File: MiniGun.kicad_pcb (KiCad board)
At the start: 2 copper layers, 111.8 x 37.5 mm, 28 parts, among them J1 JAMMA, J2 CONN_01X06, J5 PWR_IN, J6 DC2DC, J7 SCART-F, SW1 SW_Push, SW2 SW_Push, SW3 SW_Push, U1 LD1117S33TR, U2 ESP32-WROOM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

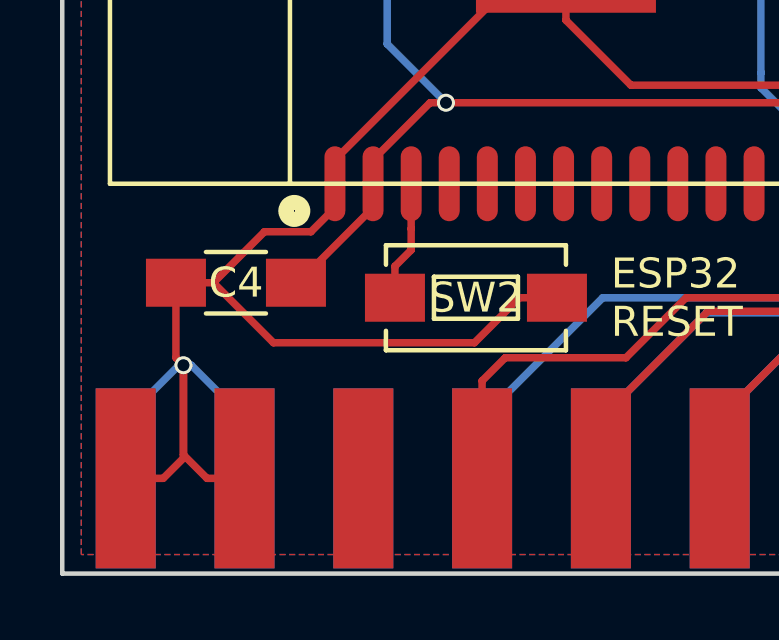
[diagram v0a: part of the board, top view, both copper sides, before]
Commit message: Added missing reset line pullup
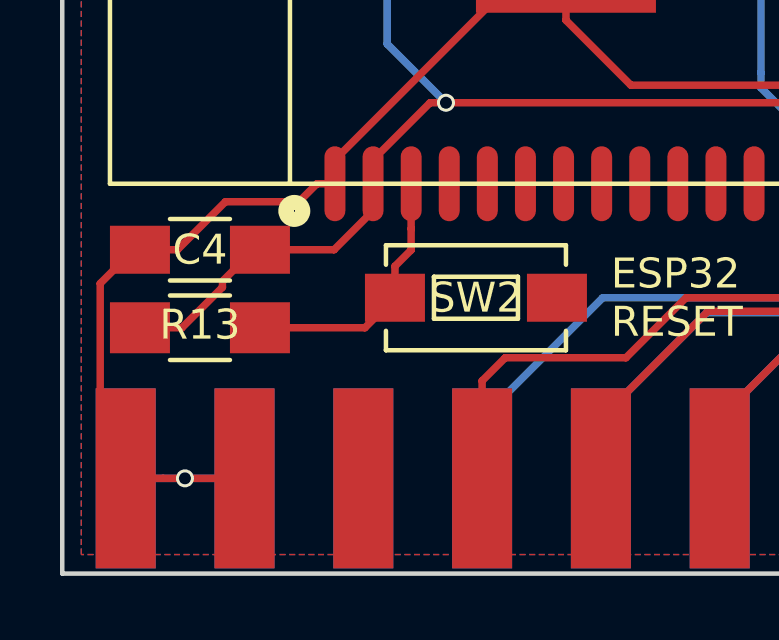
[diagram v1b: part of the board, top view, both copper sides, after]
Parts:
- added R13: 10K, Resistors_SMD:R_1206_HandSoldering, F.Cu at (97.3, 155.0)
- R11, R12: value R -> 330
- R2, R3, R4: value 330 -> 470
- moved C4 1.63 mm to (97.3, 152.4)
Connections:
- J1 pad 13: (no net) -> Net-(J1-Pad13)
- J1 pad 14: (no net) -> Net-(J1-Pad14)
- J1 pad 15: (no net) -> Net-(J1-Pad15)
- J1 pad 16: (no net) -> Net-(J1-Pad16)
- J1 pad 17: (no net) -> Net-(J1-Pad17)
- J1 pad 18: (no net) -> Net-(J1-Pad18)
- J1 pad 20: (no net) -> Net-(J1-Pad20)
- J1 pad 21: (no net) -> Net-(J1-Pad21)
- J1 pad 22: (no net) -> Net-(J1-Pad22)
- J1 pad 30: (no net) -> Net-(J1-Pad30)
- J1 pad 51: (no net) -> Net-(J1-Pad51)
- J1 pad 52: (no net) -> Net-(J1-Pad52)
- J2 pad 1: (no net) -> Net-(J2-Pad1)
- J2 pad 5: (no net) -> Net-(J2-Pad5)
- J7 pad 10: (no net) -> Net-(J7-Pad10)
- J7 pad 12: (no net) -> Net-(J7-Pad12)
- J7 pad 14: (no net) -> Net-(J7-Pad14)
- J7 pad 2: (no net) -> Net-(J7-Pad2)
- J7 pad 20: (no net) -> Net-(J7-Pad20)
- J7 pad 6: (no net) -> Net-(J7-Pad6)
- U2 pad 10: (no net) -> Net-(U2-Pad10)
- U2 pad 11: (no net) -> Net-(U2-Pad11)
- U2 pad 12: (no net) -> Net-(U2-Pad12)
- U2 pad 13: (no net) -> Net-(U2-Pad13)
- U2 pad 14: (no net) -> Net-(U2-Pad14)
- U2 pad 16: (no net) -> Net-(U2-Pad16)
- U2 pad 17: (no net) -> Net-(U2-Pad17)
- U2 pad 18: (no net) -> Net-(U2-Pad18)
- U2 pad 19: (no net) -> Net-(U2-Pad19)
- U2 pad 20: (no net) -> Net-(U2-Pad20)
- U2 pad 21: (no net) -> Net-(U2-Pad21)
- U2 pad 22: (no net) -> Net-(U2-Pad22)
- U2 pad 23: (no net) -> Net-(U2-Pad23)
- U2 pad 24: (no net) -> Net-(U2-Pad24)
- U2 pad 26: (no net) -> Net-(U2-Pad26)
- U2 pad 31: (no net) -> Net-(U2-Pad31)
- U2 pad 32: (no net) -> Net-(U2-Pad32)
- U2 pad 33: (no net) -> Net-(U2-Pad33)
- U2 pad 36: (no net) -> Net-(U2-Pad36)
- U2 pad 37: (no net) -> Net-(U2-Pad37)
- U2 pad 4: (no net) -> Net-(U2-Pad4)
- U2 pad 5: (no net) -> Net-(U2-Pad5)
- U2 pad 6: (no net) -> Net-(U2-Pad6)
- U2 pad 7: (no net) -> Net-(U2-Pad7)
- U2 pad 8: (no net) -> Net-(U2-Pad8)
- U2 pad 9: (no net) -> Net-(U2-Pad9)
- U3 pad 16: (no net) -> Net-(U3-Pad16)
- U3 pad 17: (no net) -> Net-(U3-Pad17)
- U3 pad 18: (no net) -> Net-(U3-Pad18)
- U3 pad 19: (no net) -> Net-(U3-Pad19)
- U3 pad 20: (no net) -> Net-(U3-Pad20)
- U4 pad 22: (no net) -> Net-(U4-Pad22)
- U4 pad 5: (no net) -> Net-(U4-Pad5)
- U4 pad 6: (no net) -> Net-(U4-Pad6)
- U4 pad 7: (no net) -> Net-(U4-Pad7)
- U4 pad 8: (no net) -> Net-(U4-Pad8)
- U4 pad 9: (no net) -> Net-(U4-Pad9)
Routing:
- net GND: track 312.1 -> 297.9 mm
- net 33: track 77.8 -> 84.6 mm
- net Net-(R13-Pad1): track 4.02 -> 8.94 mm
